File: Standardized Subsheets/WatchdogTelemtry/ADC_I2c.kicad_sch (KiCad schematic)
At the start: 3 parts, among them U4 MCP3428

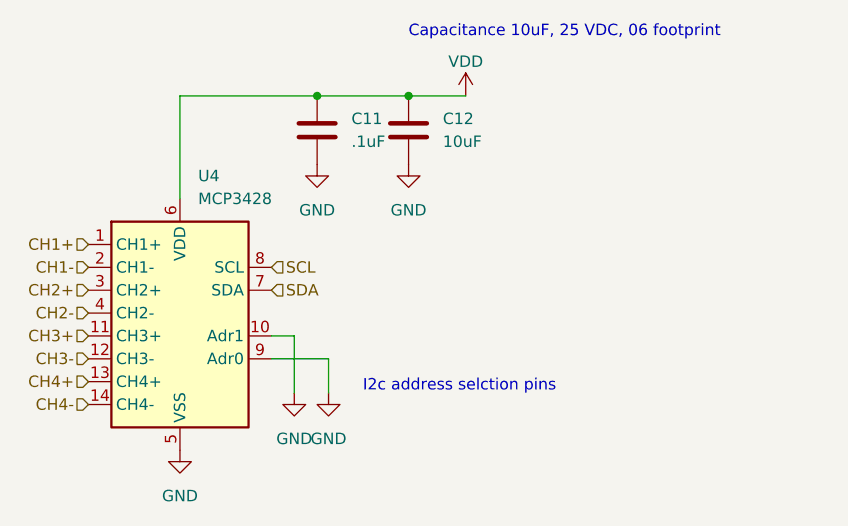
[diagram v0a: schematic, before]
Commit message: adding watchdog
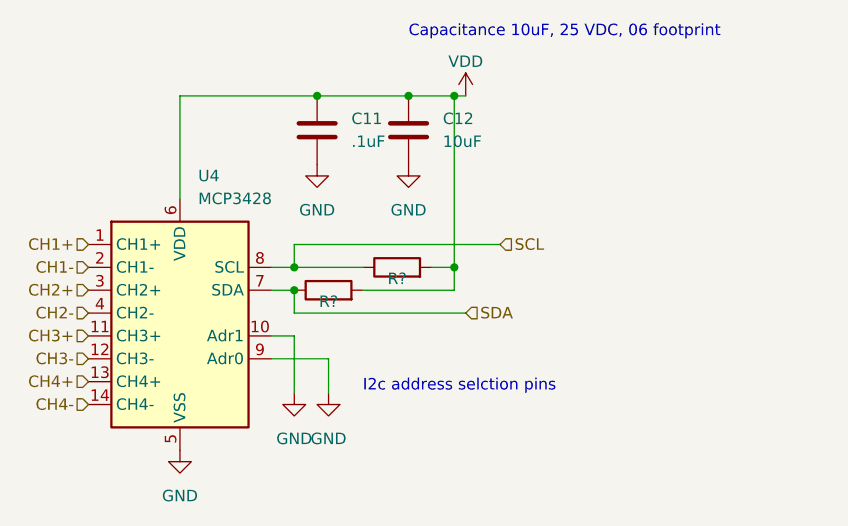
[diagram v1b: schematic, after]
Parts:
- added R? (x2): (no value), symbol Device:R
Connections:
- net SCL: now also R?.1
- net SDA: now also R?.1
- net VDD: now also R?.2, R?.2
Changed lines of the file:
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@@
   (junction (at 173.99 68.58) (diameter 0) (color 0 0 0 0)
   )
+  (junction (at 189.23 87.63) (diameter 0) (color 0 0 0 0)
+  )
+  (junction (at 171.45 87.63) (diameter 0) (color 0 0 0 0)
+  )
   (junction (at 184.15 68.58) (diameter 0) (color 0 0 0 0)
+  )
+  (junction (at 171.45 90.17) (diameter 0) (color 0 0 0 0)
+  )
+  (junction (at 189.23 68.58) (diameter 0) (color 0 0 0 0)
+  )
+  (wire (pts (xy 171.45 87.63) (xy 168.91 87.63))
+    (stroke (width 0) (type default) (color 0 0 0 0))
   )
   (wire (pts (xy 175.26 97.79) (xy 175.26 101.6))
@@
   )
   (wire (pts (xy 173.99 68.58) (xy 184.15 68.58))
+    (stroke (width 0) (type default) (color 0 0 0 0))
+  )
+  (wire (pts (xy 171.45 92.71) (xy 190.5 92.71))
     (stroke (width 0) (type default) (color 0 0 0 0))
   )
@@
     (stroke (width 0) (type default) (color 0 0 0 0))
   )
-  (wire (pts (xy 184.15 68.58) (xy 190.5 68.58))
+  (wire (pts (xy 171.45 90.17) (xy 168.91 90.17))
+    (stroke (width 0) (type default) (color 0 0 0 0))
+  )
+  (wire (pts (xy 171.45 90.17) (xy 171.45 92.71))
+    (stroke (width 0) (type default) (color 0 0 0 0))
+  )
+  (wire (pts (xy 189.23 68.58) (xy 190.5 68.58))
+    (stroke (width 0) (type default) (color 0 0 0 0))
+  )
+  (wire (pts (xy 179.07 90.17) (xy 189.23 90.17))
+    (stroke (width 0) (type default) (color 0 0 0 0))
+  )
+  (wire (pts (xy 189.23 90.17) (xy 189.23 87.63))
+    (stroke (width 0) (type default) (color 0 0 0 0))
+  )
+  (wire (pts (xy 171.45 85.09) (xy 194.31 85.09))
+    (stroke (width 0) (type default) (color 0 0 0 0))
+  )
+  (wire (pts (xy 189.23 87.63) (xy 189.23 68.58))
     (stroke (width 0) (type default) (color 0 0 0 0))
   )
   (wire (pts (xy 158.75 68.58) (xy 158.75 80.01))
+    (stroke (width 0) (type default) (color 0 0 0 0))
+  )
+  (wire (pts (xy 171.45 87.63) (xy 171.45 85.09))
+    (stroke (width 0) (type default) (color 0 0 0 0))
+  )
+  (wire (pts (xy 179.07 87.63) (xy 171.45 87.63))
+    (stroke (width 0) (type default) (color 0 0 0 0))
+  )
+  (wire (pts (xy 184.15 68.58) (xy 189.23 68.58))
+    (stroke (width 0) (type default) (color 0 0 0 0))
+  )
+  (wire (pts (xy 186.69 87.63) (xy 189.23 87.63))
     (stroke (width 0) (type default) (color 0 0 0 0))
   )
@@
     (effects (font (size 1.27 1.27)) (justify right))
   )
-  (hierarchical_label "SDA" (shape input) (at 168.91 90.17 0)
+  (hierarchical_label "SDA" (shape input) (at 190.5 92.71 0)
     (effects (font (size 1.27 1.27)) (justify left))
   )
@@
     (effects (font (size 1.27 1.27)) (justify right))
   )
-  (hierarchical_label "SCL" (shape input) (at 168.91 87.63 0)
+  (hierarchical_label "SCL" (shape input) (at 194.31 85.09 0)
     (effects (font (size 1.27 1.27)) (justify left))
   )
@@
     )
     (pin "1")
+  )
+  (symbol (lib_id "Device:R") (at 175.26 90.17 90) (unit 1)
+    (in_bom yes) (on_board yes)
+    (property "Reference" "R?" (id 0) (at 175.26 91.44 90))
+    (property "Value" "" (id 1) (at 175.26 90.17 90))
+    (property "Footprint" "" (id 2) (at 175.26 91.948 90)
+      (effects (font (size 1.27 1.27)) hide)
+    )
+    (property "Datasheet" "~" (id 3) (at 175.26 90.17 0)
+      (effects (font (size 1.27 1.27)) hide)
+    )
+    (pin "1")
+    (pin "2")
   )
   (symbol (lib_id "power:GND") (at 173.99 76.2 0) (unit 1)
@@
     (pin "1")
   )
+  (symbol (lib_id "Device:R") (at 182.88 87.63 90) (unit 1)
+    (in_bom yes) (on_board yes)
+    (property "Reference" "R?" (id 0) (at 182.88 88.9 90))
+    (property "Value" "" (id 1) (at 182.88 87.63 90))
+    (property "Footprint" "" (id 2) (at 182.88 89.408 90)
+      (effects (font (size 1.27 1.27)) hide)
+    )
+    (property "Datasheet" "~" (id 3) (at 182.88 87.63 0)
+      (effects (font (size 1.27 1.27)) hide)
+    )
+    (pin "1")
+    (pin "2")
+  )
   (symbol (lib_id "Device:C") (at 184.15 72.39 0) (unit 1)

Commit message: updated ADC and LS
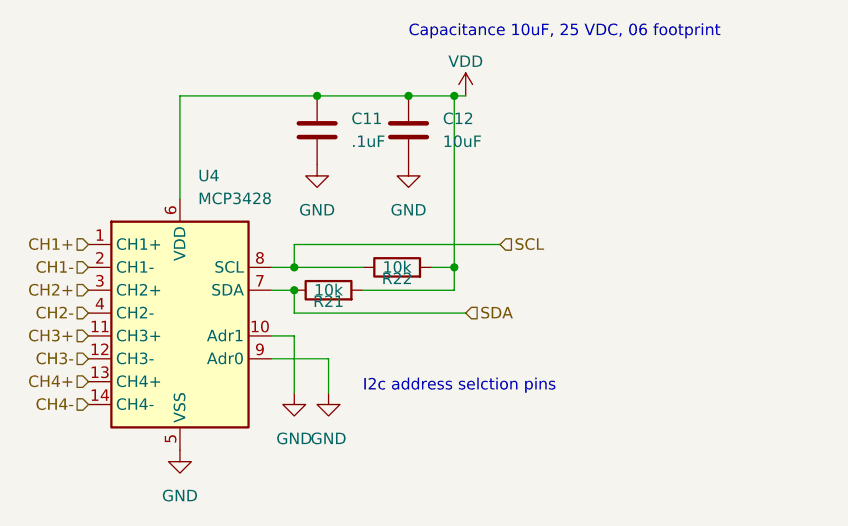
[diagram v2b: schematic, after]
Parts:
- C11, C12: footprint (none) -> Capacitor_SMD:C_0603_1608Metric
- R21, R22: renamed from R?; value (none) -> 10k; footprint (none) -> Resistor_SMD:R_0603_1608Metric
- U4: footprint (none) -> Package_SO:SOIC-14_3.9x8.7mm_P1.27mm
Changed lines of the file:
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@@
   (symbol (lib_id "Device:R") (at 175.26 90.17 90) (unit 1)
     (in_bom yes) (on_board yes)
-    (property "Reference" "R?" (id 0) (at 175.26 91.44 90))
-    (property "Value" "" (id 1) (at 175.26 90.17 90))
-    (property "Footprint" "" (id 2) (at 175.26 91.948 90)
+    (property "Reference" "R21" (id 0) (at 175.26 91.44 90))
+    (property "Value" "10k" (id 1) (at 175.26 90.17 90))
+    (property "Footprint" "Resistor_SMD:R_0603_1608Metric" (id 2) (at 175.26 91.948 90)
       (effects (font (size 1.27 1.27)) hide)
     )
@@
   (symbol (lib_id "Device:R") (at 182.88 87.63 90) (unit 1)
     (in_bom yes) (on_board yes)
-    (property "Reference" "R?" (id 0) (at 182.88 88.9 90))
-    (property "Value" "" (id 1) (at 182.88 87.63 90))
-    (property "Footprint" "" (id 2) (at 182.88 89.408 90)
+    (property "Reference" "R22" (id 0) (at 182.88 88.9 90))
+    (property "Value" "10k" (id 1) (at 182.88 87.63 90))
+    (property "Footprint" "Resistor_SMD:R_0603_1608Metric" (id 2) (at 182.88 89.408 90)
       (effects (font (size 1.27 1.27)) hide)
     )
@@
       (effects (font (size 1.27 1.27)) (justify left))
     )
-    (property "Footprint" "" (id 2) (at 185.1152 76.2 0)
+    (property "Footprint" "Capacitor_SMD:C_0603_1608Metric" (id 2) (at 185.1152 76.2 0)
       (effects (font (size 1.27 1.27)) hide)
     )
@@
       (effects (font (size 1.27 1.27)) (justify left))
     )
-    (property "Footprint" "" (id 2) (at 158.75 92.71 0)
+    (property "Footprint" "Package_SO:SOIC-14_3.9x8.7mm_P1.27mm" (id 2) (at 158.75 92.71 0)
       (effects (font (size 1.27 1.27)) hide)
     )
@@
       (effects (font (size 1.27 1.27)) (justify left))
     )
-    (property "Footprint" "" (id 2) (at 174.9552 76.2 0)
+    (property "Footprint" "Capacitor_SMD:C_0603_1608Metric" (id 2) (at 174.9552 76.2 0)
       (effects (font (size 1.27 1.27)) hide)
     )
